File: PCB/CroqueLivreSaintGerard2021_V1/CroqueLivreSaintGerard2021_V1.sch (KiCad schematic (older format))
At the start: 5 parts

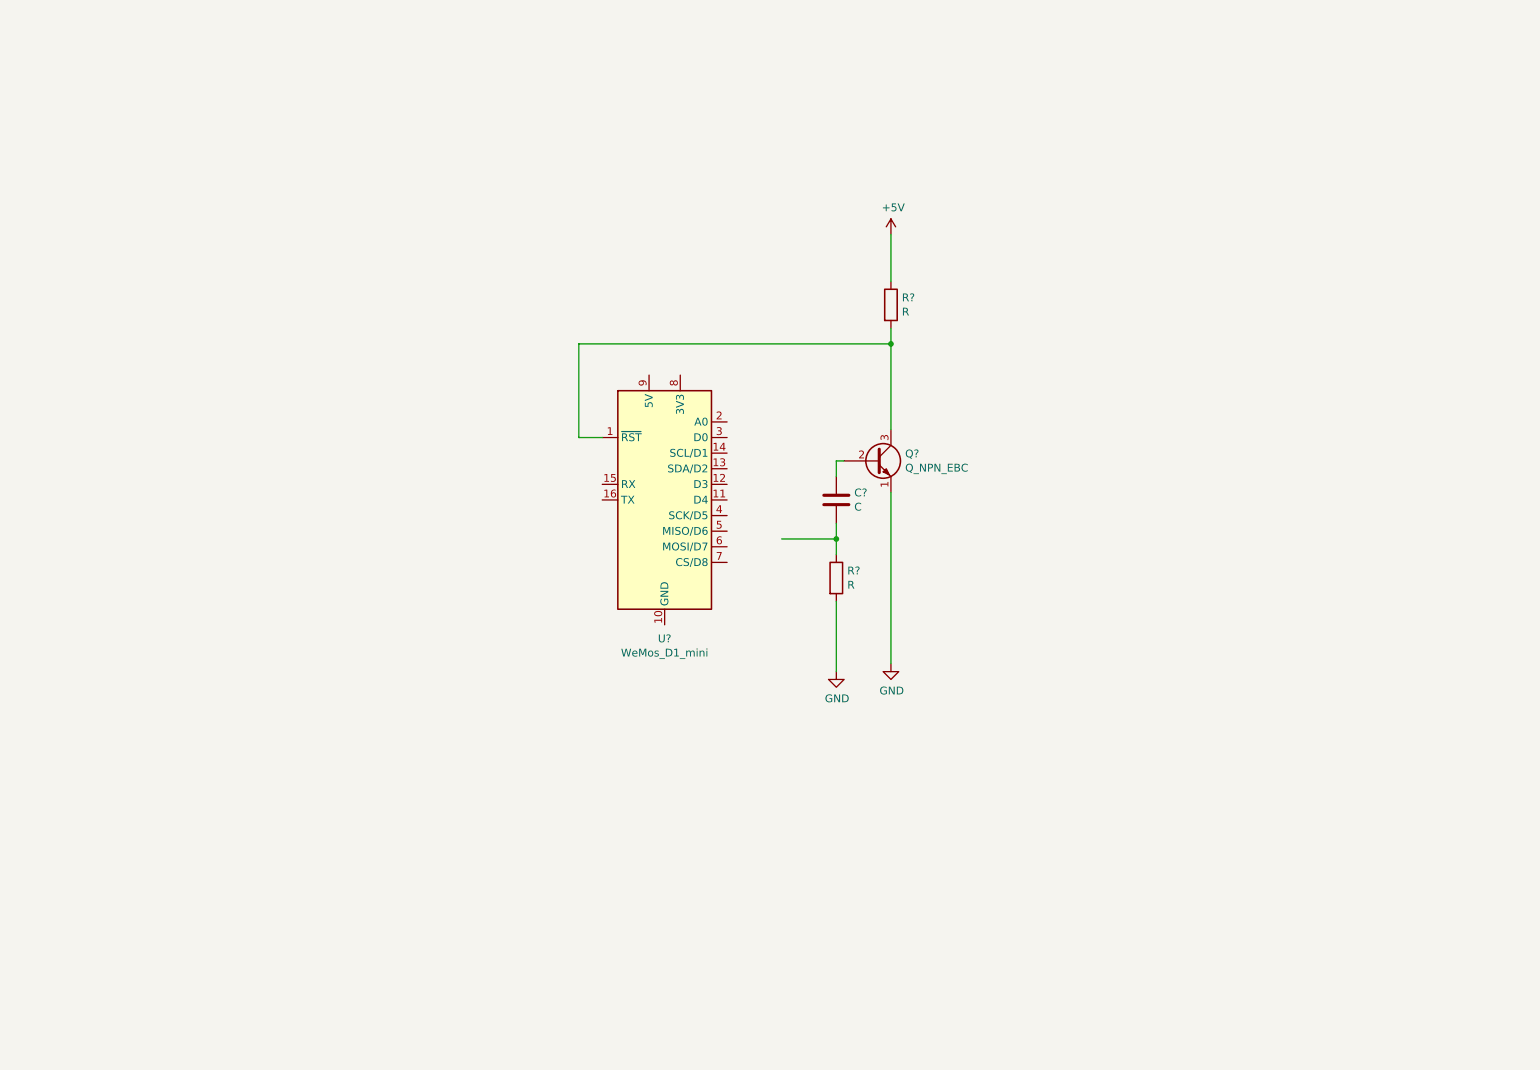
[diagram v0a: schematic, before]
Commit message: First code with all main features working with V1 electronic circuit.
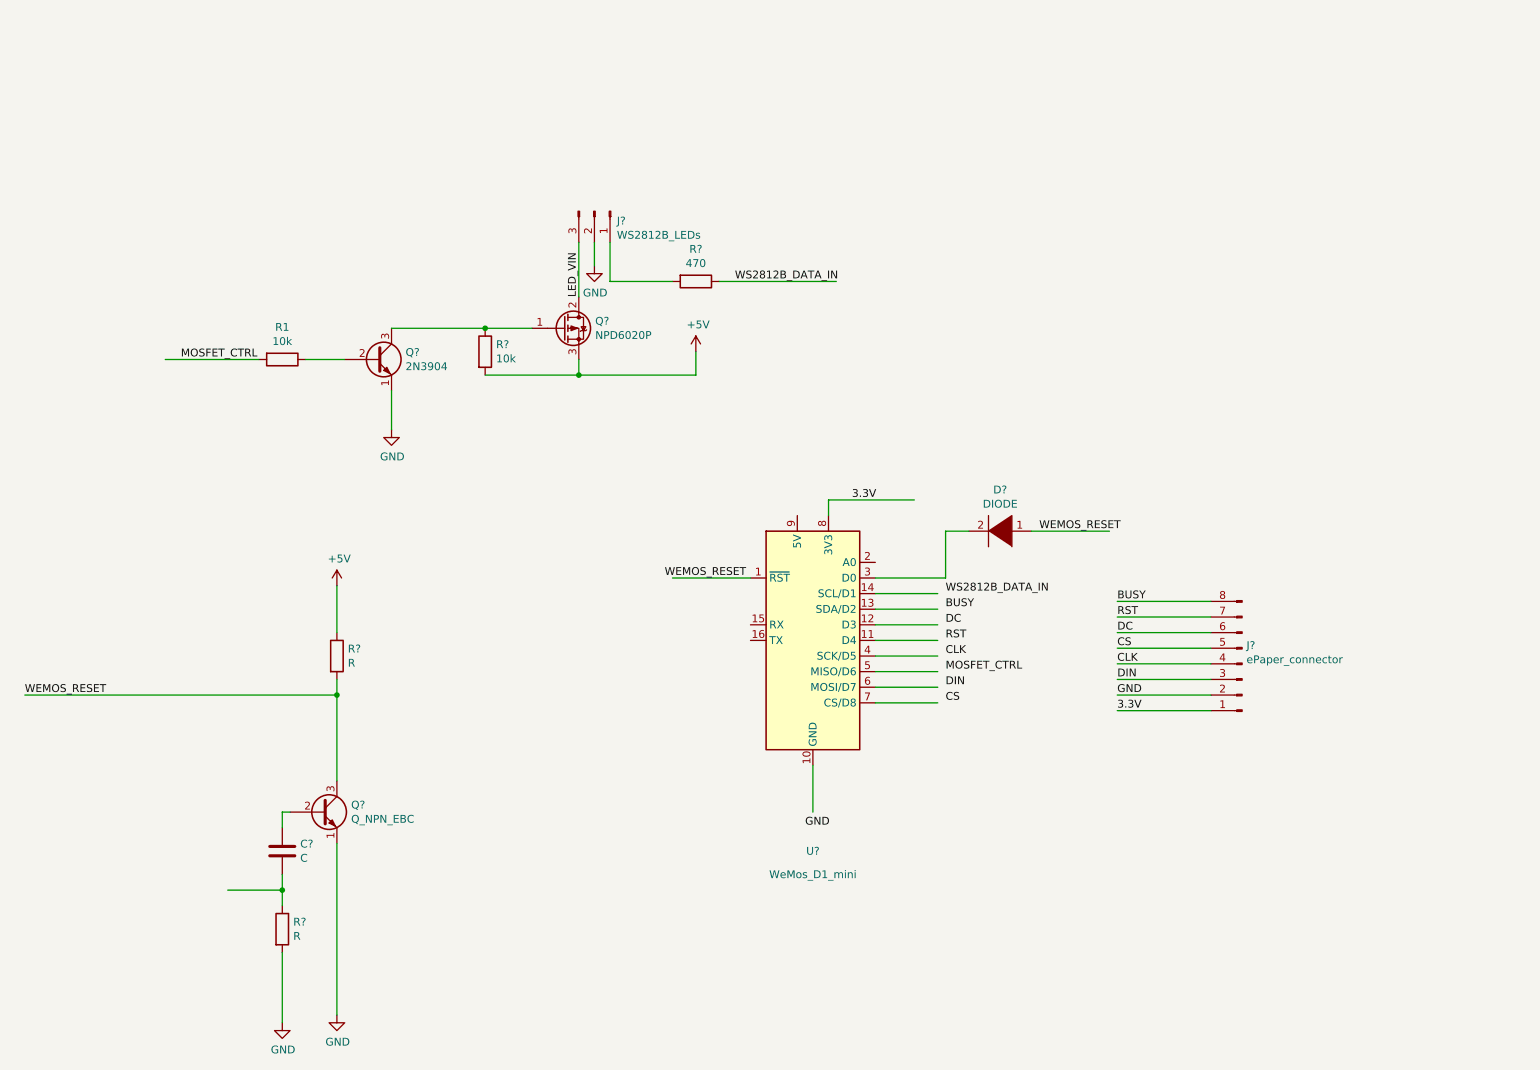
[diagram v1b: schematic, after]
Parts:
- added D?: DIODE, symbol pspice:DIODE
- added J?: ePaper_connector, symbol Connector:Conn_01x08_Male
- added J?: WS2812B_LEDs, symbol Connector:Conn_01x03_Male
- added Q?: 2N3904, symbol Device:Q_NPN_EBC
- added Q?: NPD6020P, symbol Device:Q_PMOS_GDS
- added R1, R?: 10k, symbol Device:R
- added R?: 470, symbol Device:R
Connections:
- net labels added: 3.3V, BUSY, CLK, CS, DC, DIN, LED_VIN, MOSFET_CTRL, RST, WEMOS_RESET, WS2812B_DATA_IN
- wire segments 13 -> 49
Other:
- moved on the sheet: C?, Q?, R?, U?

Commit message: Project as per the day of first release into real world!
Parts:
- removed C?: C, symbol Device:C
- removed Q?: Q_NPN_EBC, symbol Device:Q_NPN_EBC
- removed Q?: 2N3904, symbol Device:Q_NPN_EBC
- added C1: 1microF, Capacitor_THT:CP_Radial_D6.3mm_P2.50mm, symbol Device:CP
- added C2: 1000microF, lib_fp:Edge_CP_Radial_D12.5mm_P5.00mm, symbol Device:CP
- added J1: Solar pannel, Connector_JST:JST_EH_S2B-EH_1x02_P2.50mm_Horizontal, symbol Connector:Conn_01x02_Male
- added J2: TO_REED_SWICH, Connector_PinHeader_2.54mm:PinHeader_1x02_P2.54mm_Horizontal, symbol Connector:Conn_01x02_Male
- added J3: Lipo_Battery, Connector_JST:JST_EH_S2B-EH_1x02_P2.50mm_Horizontal, symbol Connector:Conn_01x02_Male
- added J4: WS2812B_LEDs_1, Connector_PinHeader_2.54mm:PinHeader_1x03_P2.54mm_Vertical, symbol Connector:Conn_01x03_Male
- added J5: WS2812B_LEDS_2, Connector_PinHeader_2.54mm:PinHeader_1x03_P2.54mm_Vertical, symbol Connector:Conn_01x03_Male
- added Q1, Q2: 2N3904, Package_TO_SOT_THT:TO-92L_Inline_Wide, symbol Device:Q_NPN_CBE
- added R2: 560, Resistor_THT:R_Axial_DIN0207_L6.3mm_D2.5mm_P10.16mm_Horizontal, symbol Device:R
- added R3: 1k, Resistor_THT:R_Axial_DIN0207_L6.3mm_D2.5mm_P10.16mm_Horizontal, symbol Device:R
- added SW1: Battery_switch, Button_Switch_THT:SW_Slide_1P2T_CK_OS102011MS2Q, symbol Switch:SW_DPST_x2
- added U1: Lithium_solar_mngt_board, Lib_fp:Lithium_solar_mngt_board, symbol Project_Library:Lithium_solar_mngt_board
- D1: renamed from D?; footprint (none) -> Diode_THT:D_DO-41_SOD81_P10.16mm_Horizontal
- J6: renamed from J?; value WS2812B_LEDs -> WS2812B_LEDs_3; footprint (none) -> Connector_PinHeader_2.54mm:PinHeader_1x03_P2.54mm_Vertical
- J7: renamed from J?; footprint (none) -> Connector_PinSocket_2.54mm:PinSocket_1x08_P2.54mm_Horizontal
- Q3: renamed from Q?; footprint (none) -> Package_TO_SOT_THT:TO-220-3_Horizontal_TabDown
- R1: renamed from R?; value R -> 560; footprint (none) -> Resistor_THT:R_Axial_DIN0207_L6.3mm_D2.5mm_P10.16mm_Horizontal
- R4: renamed from R?; value R -> 1k; footprint (none) -> Resistor_THT:R_Axial_DIN0207_L6.3mm_D2.5mm_P10.16mm_Horizontal
- R5: renamed from R1; footprint (none) -> Resistor_THT:R_Axial_DIN0207_L6.3mm_D2.5mm_P10.16mm_Horizontal
- R6, R7: renamed from R?; footprint (none) -> Resistor_THT:R_Axial_DIN0207_L6.3mm_D2.5mm_P10.16mm_Horizontal
- gave numbers to parts that had none: 1
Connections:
- net labels added: A0, D0, LED_DIN, LED_GND, LIPO+, LIPO+SWITCH, LIPO-, SOLAR+, SOLAR-
- wire segments 49 -> 78
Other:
- moved on the sheet: D1, J6, J7, Q3, R1, R4, R5, R6, R7
